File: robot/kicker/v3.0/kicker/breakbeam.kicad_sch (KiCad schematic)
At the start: 0 parts

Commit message: lots of ERC work
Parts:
- added J8, J9: Conn_01x03, Connector_JST:JST_SH_SM03B-SRSS-TB_1x03-1MP_P1.00mm_Horizontal, symbol Connector_Generic:Conn_01x03
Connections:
- new net +3V3: J8.1 (Pin_1), J9.1 (Pin_1)
- new net BB_BUS.BB_{RX}: J9.2 (Pin_2)
- new net BB_BUS.BB_{TX}: J8.2 (Pin_2)
- new net GND: J8.3 (Pin_3), J9.3 (Pin_3)
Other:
- note added: "Ball Sense Breakout"

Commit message: kicker v3.0 passing ERC
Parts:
- added J11: Conn_01x06, symbol Connector_Generic:Conn_01x06
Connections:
- net +3V3: now also J11.2 (Pin_2)
- net GND: now also J11.6 (Pin_6)
- new net +5V: J11.1 (Pin_1)
- new net BB_BUS.RST: J11.5 (Pin_5)
- new net BB_BUS.SCL: J11.4 (Pin_4)
- new net BB_BUS.SDA: J11.3 (Pin_3)
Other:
- company: (none) -> SSL A-Team
- title: (none) -> Kicker v3.0

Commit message: footprint work
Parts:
- J11: footprint (none) -> Connector_JST:JST_SH_SM06B-SRSS-TB_1x06-1MP_P1.00mm_Horizontal
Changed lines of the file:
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@@
       (effects (font (size 1.27 1.27)) (justify left))
     )
-    (property "Footprint" "" (at 101.6 40.64 0)
+    (property "Footprint" "Connector_JST:JST_SH_SM06B-SRSS-TB_1x06-1MP_P1.00mm_Horizontal" (at 101.6 40.64 0)
       (effects (font (size 1.27 1.27)) hide)
     )

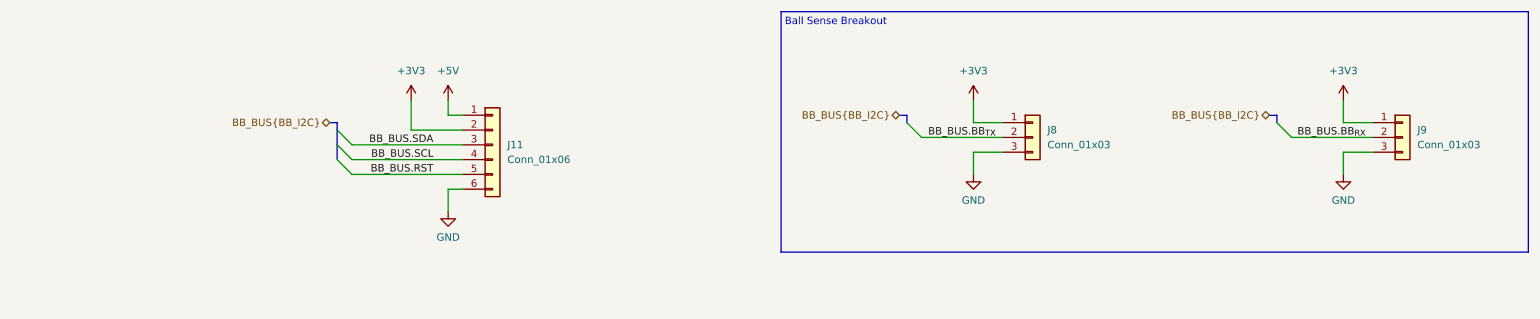
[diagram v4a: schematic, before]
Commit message: kicker v3.0 footprint work
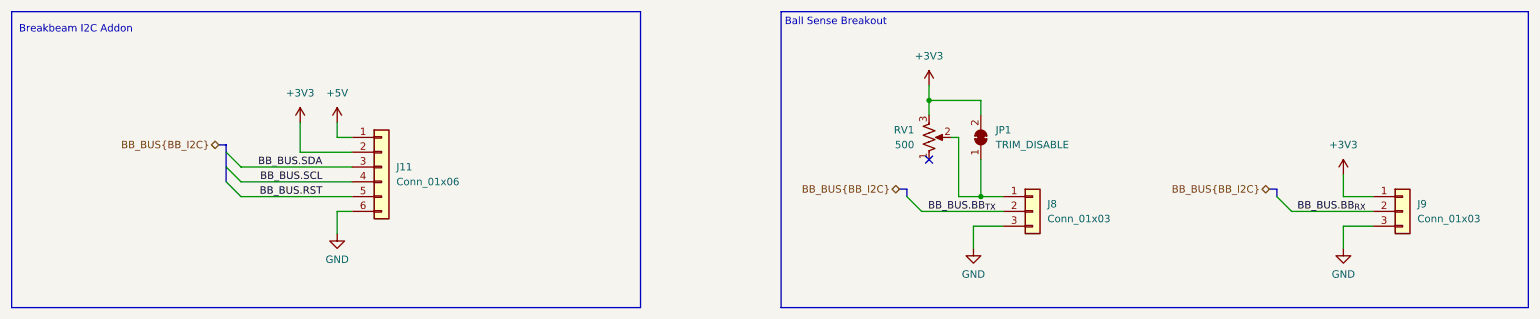
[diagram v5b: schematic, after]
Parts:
- added JP1: TRIM_DISABLE, AT-BoardFeatures:SolderJumper-2_2.0x1.2mm_Closed, symbol Jumper:SolderJumper_2_Bridged
- added RV1: 500, Potentiometer_THT:Potentiometer_Bourns_3386X_Horizontal, symbol Device:R_Potentiometer_US
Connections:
- net +3V3: now also JP1.2 (B), RV1.3; no longer J8.1 (Pin_1)
- new net: J8.1 (Pin_1), JP1.1 (A), RV1.2
- no-connect marks 0 -> 1
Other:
- note added: "Breakbeam I2C Addon"
- moved on the sheet: J11, J8, J9

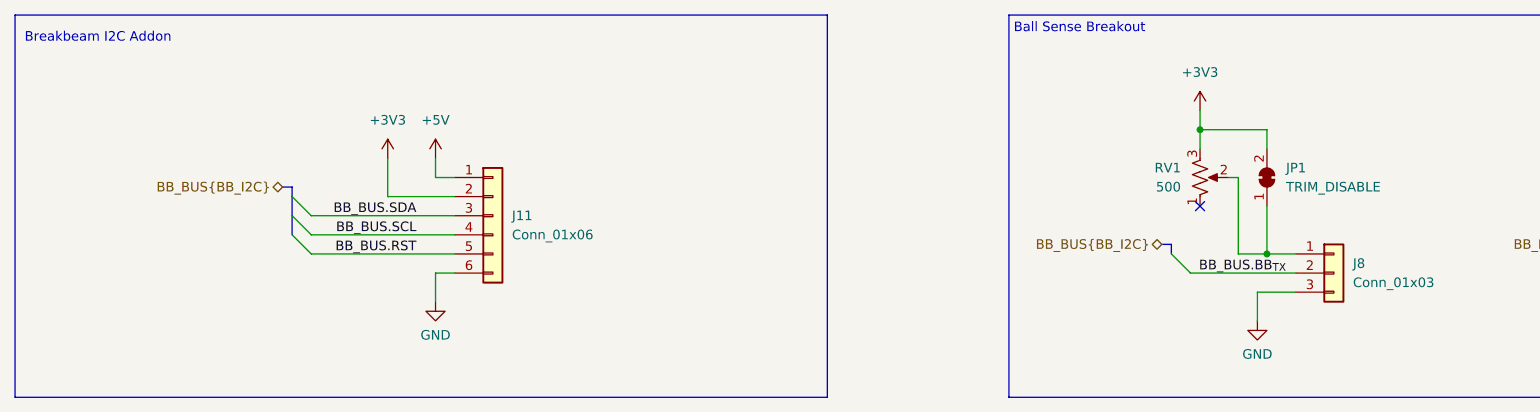
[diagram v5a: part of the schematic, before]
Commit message: kicker v3.0 changes from design review
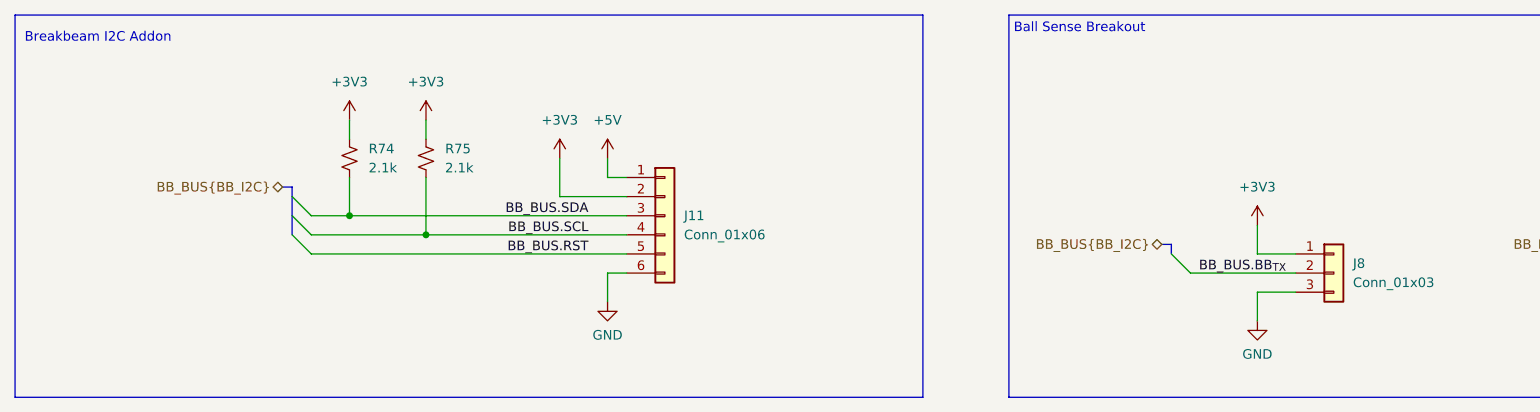
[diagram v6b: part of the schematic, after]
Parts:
- removed JP1: TRIM_DISABLE, AT-BoardFeatures:SolderJumper-2_2.0x1.2mm_Closed, symbol Jumper:SolderJumper_2_Bridged
- removed RV1: 500, Potentiometer_THT:Potentiometer_Bourns_3386X_Horizontal, symbol Device:R_Potentiometer_US
- added R74, R75: 2.1k, Resistor_SMD:R_0402_1005Metric, symbol Device:R_Small_US
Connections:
- net +3V3: now also J8.1 (Pin_1), R74.1, R75.1
- net BB_BUS.SCL: now also R75.2
- net BB_BUS.SDA: now also R74.2
- no-connect marks 1 -> 0
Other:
- moved on the sheet: J11

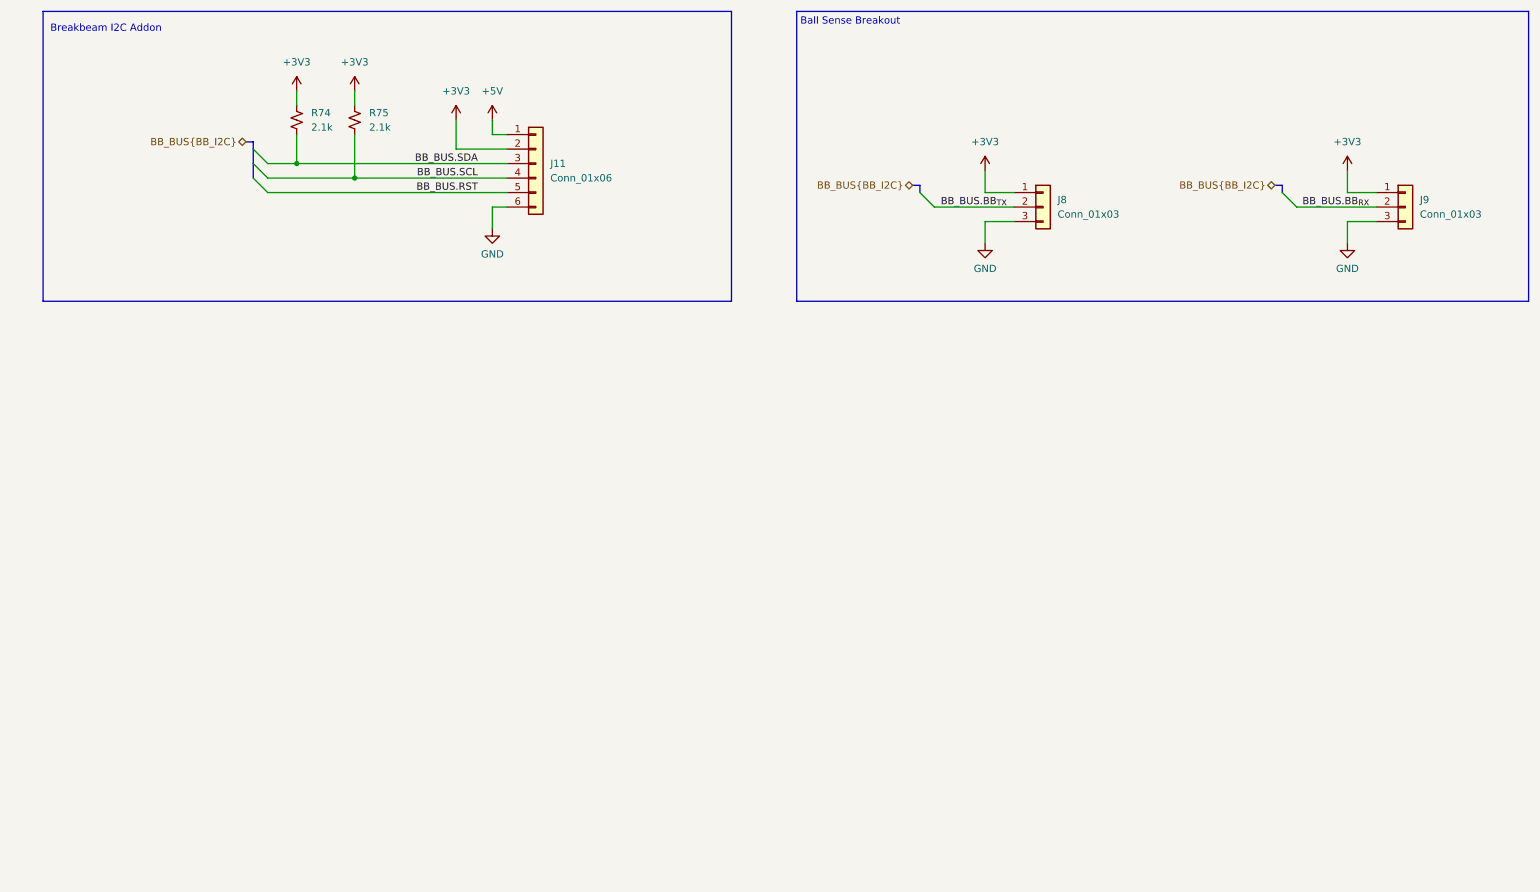
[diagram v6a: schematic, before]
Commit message: updating schematic to stm32f407 100pin
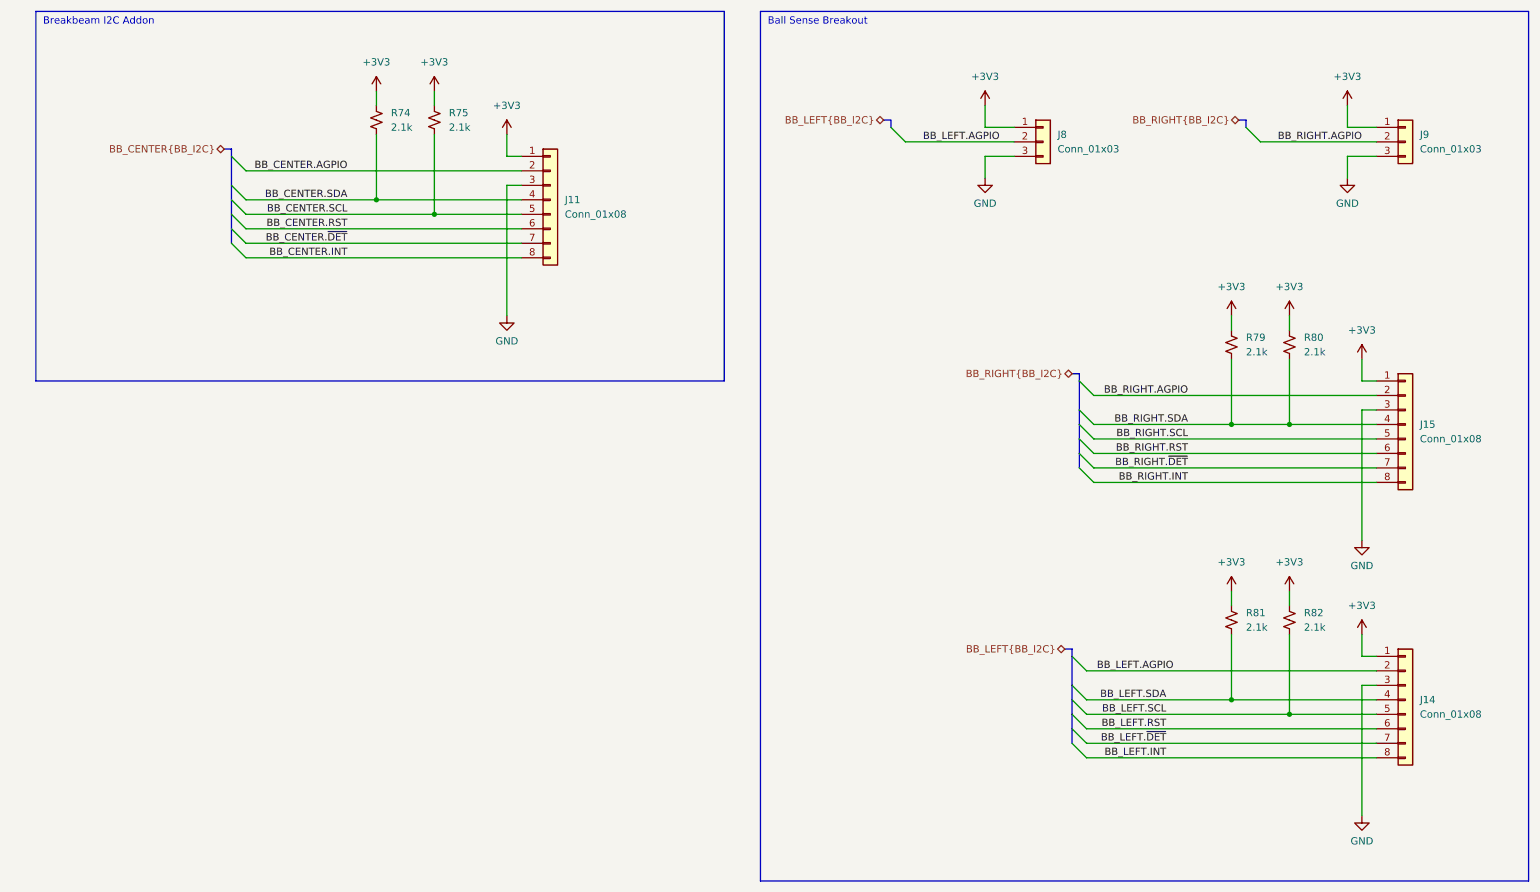
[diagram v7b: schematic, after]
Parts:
- removed J11: Conn_01x06, Connector_JST:JST_SH_SM06B-SRSS-TB_1x06-1MP_P1.00mm_Horizontal, symbol Connector_Generic:Conn_01x06
- added J11, J14, J15: Conn_01x08, symbol Connector_Generic:Conn_01x08
- added R79, R80, R81, R82: 2.1k, Resistor_SMD:R_0402_1005Metric, symbol Device:R_Small_US
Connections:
- net +3V3: now also J11.1 (Pin_1), J14.1 (Pin_1), J15.1 (Pin_1), R79.1, R80.1, R81.1, R82.1
- net GND: now also J11.3 (Pin_3), J14.3 (Pin_3), J15.3 (Pin_3)
- net BB_BUS.BB_{RX} renamed BB_RIGHT.AGPIO
- net BB_RIGHT.AGPIO: now also J15.2 (Pin_2)
- net BB_BUS.BB_{TX} renamed BB_LEFT.AGPIO
- net BB_LEFT.AGPIO: now also J14.2 (Pin_2)
- net BB_BUS.SCL renamed BB_CENTER.SCL
- net BB_CENTER.SCL: now also J11.5 (Pin_5)
- net BB_BUS.SDA renamed BB_CENTER.SDA
- net BB_CENTER.SDA: now also J11.4 (Pin_4)
- new net BB_CENTER.AGPIO: J11.2 (Pin_2)
- new net BB_CENTER.INT: J11.8 (Pin_8)
- new net BB_CENTER.RST: J11.6 (Pin_6)
- new net BB_CENTER.~{DET}: J11.7 (Pin_7)
- new net BB_LEFT.INT: J14.8 (Pin_8)
- new net BB_LEFT.RST: J14.6 (Pin_6)
- new net BB_LEFT.SCL: J14.5 (Pin_5), R82.2
- new net BB_LEFT.SDA: J14.4 (Pin_4), R81.2
- new net BB_LEFT.~{DET}: J14.7 (Pin_7)
- new net BB_RIGHT.INT: J15.8 (Pin_8)
- new net BB_RIGHT.RST: J15.6 (Pin_6)
- new net BB_RIGHT.SCL: J15.5 (Pin_5)
- new net BB_RIGHT.SDA: J15.4 (Pin_4), R79.2, R80.2
- new net BB_RIGHT.~{DET}: J15.7 (Pin_7)
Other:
- moved on the sheet: J8, J9, R74, R75

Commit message: lots of kicker work
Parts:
- J11, J14, J15: footprint (none) -> Connector_JST:JST_SH_SM08B-SRSS-TB_1x08-1MP_P1.00mm_Horizontal
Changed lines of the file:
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@@
     (effects (font (size 1.27 1.27)) (justify right bottom))
   )
-  (label "BB_RIGHT.AGPIO" (at 250.19 40.64 180)
-    (effects (font (size 1.27 1.27)) (justify right bottom))
-  )
-  (label "BB_RIGHT.INT" (at 219.71 100.33 180)
-    (effects (font (size 1.27 1.27)) (justify right bottom))
-  )
-  (label "BB_CENTER.RST" (at 72.39 55.88 180)
-    (effects (font (size 1.27 1.27)) (justify right bottom))
-  )
-  (label "BB_CENTER.~{DET}" (at 72.39 58.42 180)
-    (effects (font (size 1.27 1.27)) (justify right bottom))
-  )
-  (label "BB_RIGHT.SCL" (at 219.71 92.71 180)
-    (effects (font (size 1.27 1.27)) (justify right bottom))
-  )
-  (label "BB_LEFT.SDA" (at 215.9 138.43 180)
-    (effects (font (size 1.27 1.27)) (justify right bottom))
-  )
-  (label "BB_LEFT.AGPIO" (at 186.69 40.64 180)
-    (effects (font (size 1.27 1.27)) (justify right bottom))
-  )
-  (label "BB_CENTER.SDA" (at 72.39 50.8 180)
-    (effects (font (size 1.27 1.27)) (justify right bottom))
-  )
-  (label "BB_LEFT.~{DET}" (at 215.9 146.05 180)
-    (effects (font (size 1.27 1.27)) (justify right bottom))
-  )
-  (label "BB_RIGHT.~{DET}" (at 219.71 97.79 180)
-    (effects (font (size 1.27 1.27)) (justify right bottom))
-  )
-  (label "BB_CENTER.AGPIO" (at 72.39 45.72 180)
-    (effects (font (size 1.27 1.27)) (justify right bottom))
-  )
-  (label "BB_LEFT.SCL" (at 215.9 140.97 180)
-    (effects (font (size 1.27 1.27)) (justify right bottom))
-  )
-  (label "BB_LEFT.RST" (at 215.9 143.51 180)
-    (effects (font (size 1.27 1.27)) (justify right bottom))
-  )
-  (label "BB_CENTER.SCL" (at 72.39 53.34 180)
-    (effects (font (size 1.27 1.27)) (justify right bottom))
-  )
-  (label "BB_CENTER.INT" (at 72.39 60.96 180)
-    (effects (font (size 1.27 1.27)) (justify right bottom))
-  )
-  (label "BB_RIGHT.SDA" (at 219.71 90.17 180)
-    (effects (font (size 1.27 1.27)) (justify right bottom))
-  )
-  (label "BB_LEFT.INT" (at 215.9 148.59 180)
-    (effects (font (size 1.27 1.27)) (justify right bottom))
-  )
-  (label "BB_RIGHT.RST" (at 219.71 95.25 180)
+  (label "BB_RIGHT.AGPIO" (at 250.19 40.64 180) (fields_autoplaced)
+    (effects (font (size 1.27 1.27)) (justify right bottom))
+  )
+  (label "BB_RIGHT.INT" (at 219.71 100.33 180) (fields_autoplaced)
+    (effects (font (size 1.27 1.27)) (justify right bottom))
+  )
+  (label "BB_CENTER.RST" (at 72.39 55.88 180) (fields_autoplaced)
+    (effects (font (size 1.27 1.27)) (justify right bottom))
+  )
+  (label "BB_CENTER.~{DET}" (at 72.39 58.42 180) (fields_autoplaced)
+    (effects (font (size 1.27 1.27)) (justify right bottom))
+  )
+  (label "BB_RIGHT.SCL" (at 219.71 92.71 180) (fields_autoplaced)
+    (effects (font (size 1.27 1.27)) (justify right bottom))
+  )
+  (label "BB_LEFT.SDA" (at 215.9 138.43 180) (fields_autoplaced)
+    (effects (font (size 1.27 1.27)) (justify right bottom))
+  )
+  (label "BB_LEFT.AGPIO" (at 186.69 40.64 180) (fields_autoplaced)
+    (effects (font (size 1.27 1.27)) (justify right bottom))
+  )
+  (label "BB_CENTER.SDA" (at 72.39 50.8 180) (fields_autoplaced)
+    (effects (font (size 1.27 1.27)) (justify right bottom))
+  )
+  (label "BB_LEFT.~{DET}" (at 215.9 146.05 180) (fields_autoplaced)
+    (effects (font (size 1.27 1.27)) (justify right bottom))
+  )
+  (label "BB_RIGHT.~{DET}" (at 219.71 97.79 180) (fields_autoplaced)
+    (effects (font (size 1.27 1.27)) (justify right bottom))
+  )
+  (label "BB_CENTER.AGPIO" (at 72.39 45.72 180) (fields_autoplaced)
+    (effects (font (size 1.27 1.27)) (justify right bottom))
+  )
+  (label "BB_LEFT.SCL" (at 215.9 140.97 180) (fields_autoplaced)
+    (effects (font (size 1.27 1.27)) (justify right bottom))
+  )
+  (label "BB_LEFT.RST" (at 215.9 143.51 180) (fields_autoplaced)
+    (effects (font (size 1.27 1.27)) (justify right bottom))
+  )
+  (label "BB_CENTER.SCL" (at 72.39 53.34 180) (fields_autoplaced)
+    (effects (font (size 1.27 1.27)) (justify right bottom))
+  )
+  (label "BB_CENTER.INT" (at 72.39 60.96 180) (fields_autoplaced)
+    (effects (font (size 1.27 1.27)) (justify right bottom))
+  )
+  (label "BB_RIGHT.SDA" (at 219.71 90.17 180) (fields_autoplaced)
+    (effects (font (size 1.27 1.27)) (justify right bottom))
+  )
+  (label "BB_LEFT.INT" (at 215.9 148.59 180) (fields_autoplaced)
+    (effects (font (size 1.27 1.27)) (justify right bottom))
+  )
+  (label "BB_RIGHT.RST" (at 219.71 95.25 180) (fields_autoplaced)
     (effects (font (size 1.27 1.27)) (justify right bottom))
   )
@@
       (effects (font (size 1.27 1.27)) (justify left))
     )
-    (property "Footprint" "" (at 257.81 90.17 0)
+    (property "Footprint" "Connector_JST:JST_SH_SM08B-SRSS-TB_1x08-1MP_P1.00mm_Horizontal" (at 257.81 90.17 0)
       (effects (font (size 1.27 1.27)) hide)
     )
@@
       (effects (font (size 1.27 1.27)) (justify left))
     )
-    (property "Footprint" "" (at 257.81 138.43 0)
+    (property "Footprint" "Connector_JST:JST_SH_SM08B-SRSS-TB_1x08-1MP_P1.00mm_Horizontal" (at 257.81 138.43 0)
       (effects (font (size 1.27 1.27)) hide)
     )
@@
       (effects (font (size 1.27 1.27)) (justify left))
     )
-    (property "Footprint" "" (at 107.95 50.8 0)
-      (effects (font (size 1.27 1.27)) hide)
-    )
+    (property "Footprint" "Connector_JST:JST_SH_SM08B-SRSS-TB_1x08-1MP_P1.00mm_Horizontal" (at 107.95 50.8 0)
+      (effects (font (size 1.27 1.27)) hide)
+    )
